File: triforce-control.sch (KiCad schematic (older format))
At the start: 21 parts, among them U1 ADAFRUIT_HUZZAH, U2 bno055, U3 LPC1768

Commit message: Started new PCB design.
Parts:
- removed CON_D1: Drive Motor 1, mbed:AngledServoCon, symbol Servo
- removed CON_D2: Drive Motor 2, mbed:AngledServoCon, symbol Servo
- removed CON_D3: Drive Motor 3, mbed:AngledServoCon, symbol Servo
- removed CON_RX_D1: Drive Chan 1, mbed:AngledServoCon, symbol Servo
- removed CON_RX_D2: Drive Chan 2, mbed:AngledServoCon, symbol Servo
- removed CON_RX_D3: Drive Chan 3, mbed:AngledServoCon, symbol Servo
- removed CON_RX_D4: Drive Chan 4, mbed:AngledServoCon, symbol Servo
- removed CON_RX_D5: Drive Chan 5, mbed:AngledServoCon, symbol Servo
- removed CON_RX_D6: Drive Chan 6, mbed:AngledServoCon, symbol Servo
- removed CON_RX_W1: Weapon Chan 1, mbed:AngledServoCon, symbol Servo
- removed CON_RX_W2: Weapon Chan 2, mbed:AngledServoCon, symbol Servo
- removed CON_RX_W3: Weapon Chan 3, mbed:AngledServoCon, symbol Servo
- removed CON_RX_W4: Weapon Chan 4, mbed:AngledServoCon, symbol Servo
- removed CON_RX_W5: Weapon Chan 5, mbed:AngledServoCon, symbol Servo
- removed CON_RX_W6: Weapon Chan 6, mbed:AngledServoCon, symbol Servo
- removed CON_W1, CON_W2, CON_W3: Weapon Motor 1, mbed:AngledServoCon, symbol Servo
- added CON1, CON2: Conn_01x08, Connectors_JST:JST_PH_S8B-PH-K_08x2.00mm_Angled, symbol Conn_01x08
- added CON3: CON_ESC_W1, mbed:Pin_Header_Angled_3x01_Pitch2.54mm, symbol Conn_01x03
- added CON4: CON_ESC_W2, mbed:Pin_Header_Angled_3x01_Pitch2.54mm, symbol Conn_01x03
- added CON5: CON_ESC_W3, mbed:Pin_Header_Angled_3x01_Pitch2.54mm, symbol Conn_01x03
- added CON6: CON_ESC_D1, mbed:Pin_Header_Angled_3x01_Pitch2.54mm, symbol Conn_01x03
- added CON7: CON_ESC_D2, mbed:Pin_Header_Angled_3x01_Pitch2.54mm, symbol Conn_01x03
- added CON8: CON_ESC_D3, mbed:Pin_Header_Angled_3x01_Pitch2.54mm, symbol Conn_01x03
- added CON9: Conn_01x04, Connectors_JST:JST_PH_S4B-PH-K_04x2.00mm_Angled, symbol Conn_01x04
- added U4: SN65HVD232, Housings_SOIC:SOIC-8_3.9x4.9mm_Pitch1.27mm, symbol SN65HVD232
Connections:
- net +5V: now also CON1.2 (Pin_2), CON2.2 (Pin_2), CON3.2 (Pin_2), CON4.2 (Pin_2), CON5.2 (Pin_2), CON6.2 (Pin_2), CON7.2 (Pin_2), CON8.2 (Pin_2), CON9.4 (Pin_4)
- net ESP_READY: now also U3.19 (GPIO_19); no longer U3.29 (td)
- net GND: now also CON1.1 (Pin_1), CON2.1 (Pin_1), CON3.1 (Pin_1), CON4.1 (Pin_1), CON5.1 (Pin_1), CON6.1 (Pin_1), CON7.1 (Pin_1), CON8.1 (Pin_1), CON9.1 (Pin_1), U4.2 (GND)
- net IN_RX_D1: now also CON1.3 (Pin_3)
- net IN_RX_D2: now also CON1.4 (Pin_4)
- net IN_RX_D3: now also CON1.5 (Pin_5)
- net IN_RX_D4: now also CON1.6 (Pin_6)
- net IN_RX_D5: now also CON1.7 (Pin_7)
- net IN_RX_D6: now also CON1.8 (Pin_8)
- net IN_RX_W1: now also U3.12 (miso), CON2.3 (Pin_3); no longer U3.5 (mosi)
- net IN_RX_W2: now also U3.11 (mosi), CON2.4 (Pin_4); no longer U3.6 (miso)
- net IN_RX_W3: now also U3.8 (GPIO_8), CON2.5 (Pin_5); no longer U3.7 (sck)
- net IN_RX_W4: now also U3.7 (sck), CON2.6 (Pin_6); no longer U3.8 (GPIO_8)
- net IN_RX_W5: now also U3.6 (miso), CON2.7 (Pin_7); no longer U3.11 (mosi)
- net IN_RX_W6: now also U3.5 (mosi), CON2.8 (Pin_8); no longer U3.12 (miso)
- net PWM_OUT_DRV_MOTOR_1: now also U3.23 (GPIO_23), CON6.3 (Pin_3); no longer U3.21 (GPIO_21)
- net PWM_OUT_DRV_MOTOR_2: now also CON7.3 (Pin_3)
- net PWM_OUT_DRV_MOTOR_3: now also U3.21 (GPIO_21), CON8.3 (Pin_3); no longer U3.23 (GPIO_23)
- net PWM_OUT_WPN_MOTOR_1: now also U3.26 (GPIO_26), CON3.3 (Pin_3); no longer U3.24 (GPIO_24)
- net PWM_OUT_WPN_MOTOR_2: now also CON4.3 (Pin_3)
- net PWM_OUT_WPN_MOTOR_3: now also U3.24 (GPIO_24), CON5.3 (Pin_3); no longer U3.26 (GPIO_26)
- net CAN_RXD: now reaches U3.30 (rd)
- net CAN_RXD: now also U4.4 (R)
- net MBED_3V3: now reaches U3.40 (VOUT)
- net MBED_3V3: now also U4.3 (VCC)
- new net CAN_H: CON9.3 (Pin_3), U4.7 (CANH)
- new net CAN_L: CON9.2 (Pin_2), U4.6 (CANL)
- new net CAN_TXD: U3.29 (td), U4.1 (D)
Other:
- note added: "CAN Transceiver"
- note added: "ESC Connections"
- note added: "Main MCU"
- note added: "Orientation Sensor"
- note added: "RF Receiver Connections"
- note added: "WiFi MCU"
- moved on the sheet: U1, U2, U3

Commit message: Swapped JSP PH for JST SH on RX inputs.
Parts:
- CON1, CON2: footprint Connectors_JST:JST_PH_S8B-PH-K_08x2.00mm_Angled -> Connectors_JST:JST_SH_SM08B-SRSS-TB_08x1.00mm_Angled
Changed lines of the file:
@@
 F 0 "CON1" H 9100 4300 50  0000 C CNN
 F 1 "Conn_01x08" H 9100 3400 50  0000 C CNN
-F 2 "Connectors_JST:JST_PH_S8B-PH-K_08x2.00mm_Angled" H 9100 3900 50  0001 C CNN
+F 2 "Connectors_JST:JST_SH_SM08B-SRSS-TB_08x1.00mm_Angled" H 9100 3900 50  0001 C CNN
 F 3 "" H 9100 3900 50  0001 C CNN
 	1    9100 3900
@@
 F 0 "CON2" H 10050 4300 50  0000 C CNN
 F 1 "Conn_01x08" H 10050 3400 50  0000 C CNN
-F 2 "Connectors_JST:JST_PH_S8B-PH-K_08x2.00mm_Angled" H 10050 3900 50  0001 C CNN
+F 2 "Connectors_JST:JST_SH_SM08B-SRSS-TB_08x1.00mm_Angled" H 10050 3900 50  0001 C CNN
 F 3 "" H 10050 3900 50  0001 C CNN
 	1    10050 3900

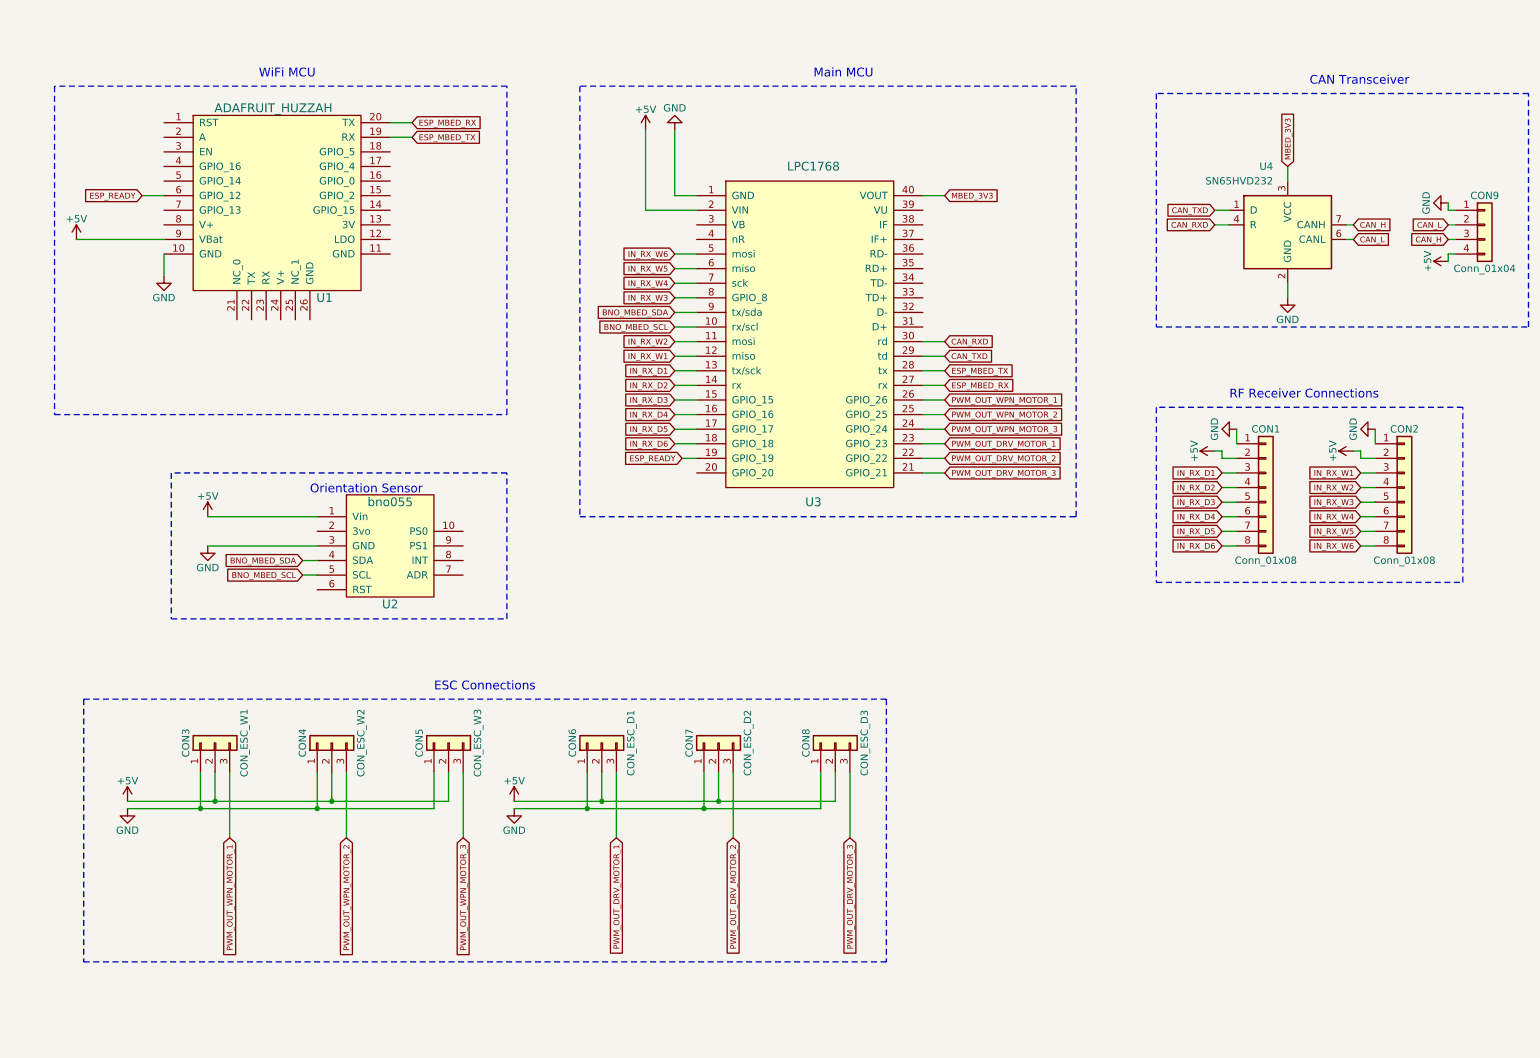
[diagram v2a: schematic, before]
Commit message: Connected an extra ESP8266 ground pin.
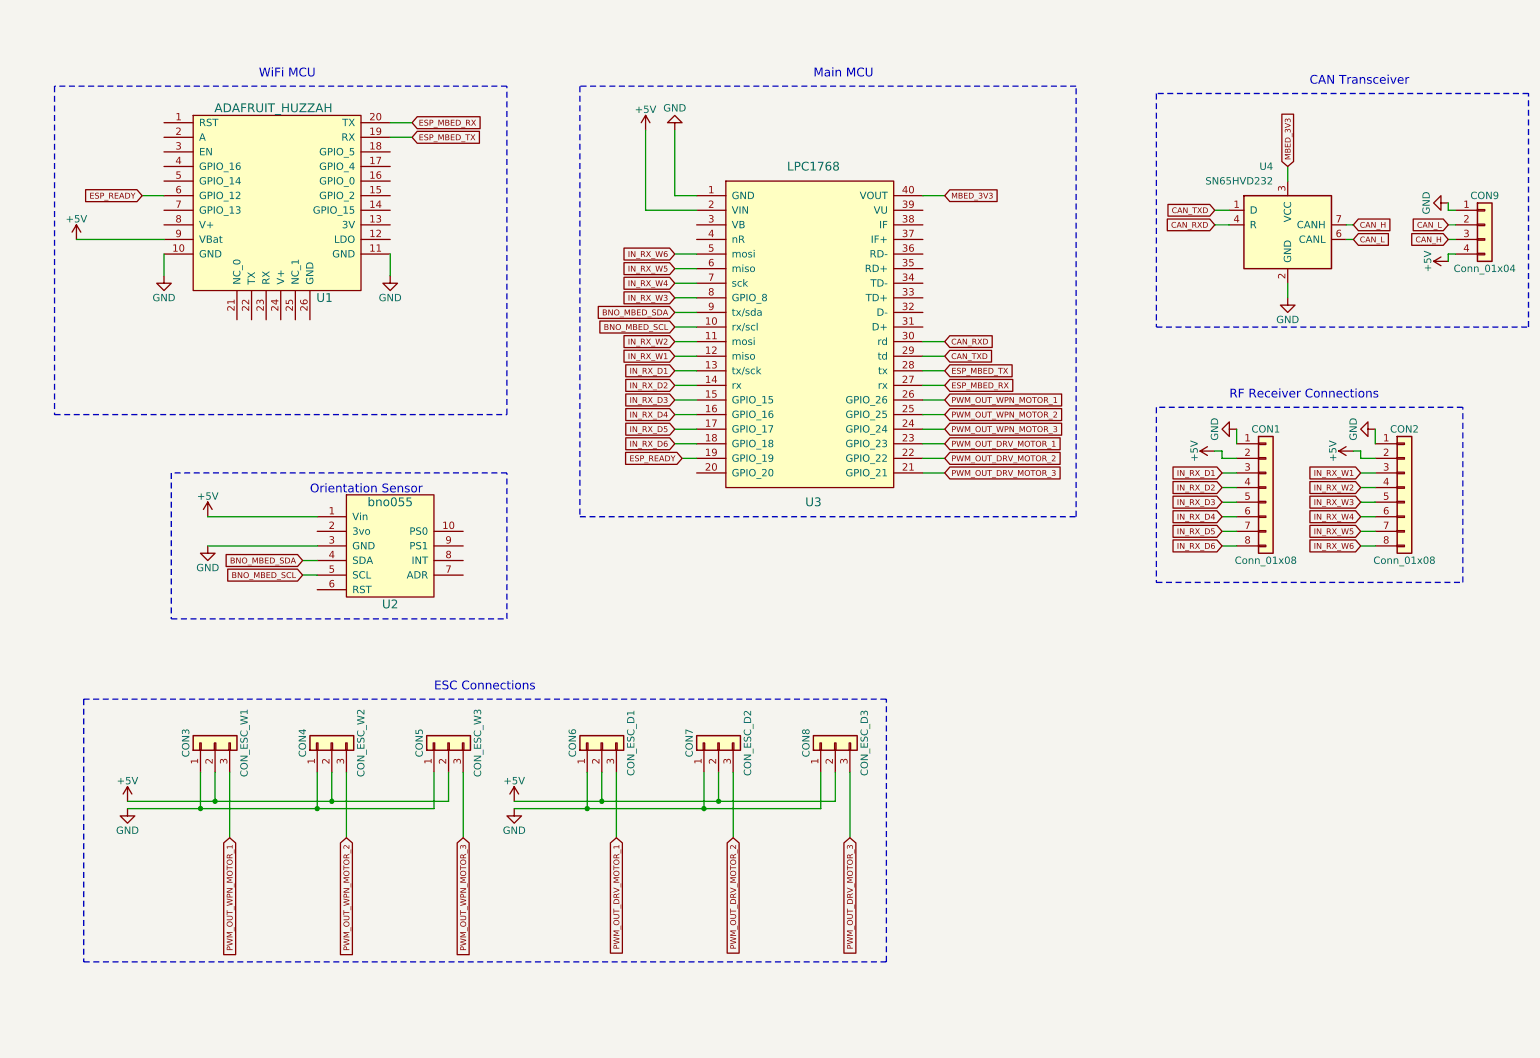
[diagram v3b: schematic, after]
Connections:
- net GND: now also U1.11 (GND)
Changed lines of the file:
@@
 	1000 7150 6500 7150
 Wire Notes Line
-	6500 5350 6500 7150
+	6500 7150 6500 5350
 Wire Notes Line
-	1000 5350 6500 5350
+	6500 5350 1000 5350
 Text Notes 3400 5300 0    60   ~ 0
 ESC Connections
+$Comp
+L GND #PWR?
+U 1 1 5A6239A5
+P 3100 2450
+F 0 "#PWR?" H 3100 2200 50  0001 C CNN
+F 1 "GND" H 3100 2300 50  0000 C CNN
+F 2 "" H 3100 2450 50  0001 C CNN
+F 3 "" H 3100 2450 50  0001 C CNN
+	1    3100 2450
+	1    0    0    -1
+$EndComp
+Wire Wire Line
+	3100 2450 3100 2300
 $EndSCHEMATC
